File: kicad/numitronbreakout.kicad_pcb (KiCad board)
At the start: 2 copper layers, 25 parts, among them J1 Conn_01x06, U1 HV5812WG-G, U2 IV-12, U3 IV-12, U4 LM317_TO-220, U5 TPS61391RTER

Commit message: boost converter refactor
new design from web bench to reduce bom complexity & increase efficiency
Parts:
- removed Capd1: 470 pF, Capacitor_SMD:C_0402_1005Metric
- removed Cavcc1: 1.0 μF, Capacitor_SMD:C_0603_1608Metric
- removed Ccap1: 4.7 nF, Capacitor_SMD:C_0402_1005Metric
- removed Cin1: 1.0 μF, Capacitor_SMD:C_0402_1005Metric
- removed Cmon1, Cmon2: 10.0 pF, Capacitor_SMD:C_0201_0603Metric
- removed Cout1: 100 nF, Capacitor_SMD:C_0603_1608Metric
- removed D1: VF@Io = 1.0 V / VRRM = 100.0 V, Diode_SMD:D_SOD-123
- removed L1: 4.7 μH, Inductor_SMD:L_1008_2520Metric
- removed Ren1, Risshort1: 100 kΩ, Resistor_SMD:R_0402_1005Metric
- removed Rfbb1: 10 kΩ, Resistor_SMD:R_0402_1005Metric
- removed Rfbt1: 240 kΩ, Resistor_SMD:R_0603_1608Metric
- removed Rmon1, Rmon2: 3.01 kΩ, Resistor_SMD:R_0402_1005Metric
- removed Rvcc1: 10 Ω, Resistor_SMD:R_0402_1005Metric
- removed U5: TPS61391RTER, NewFootprints:RTE0016C
- added U7: LM2733XMF, Package_TO_SOT_SMD:SOT-23-5, F.Cu at (208.4, 71.5)
- moved U4 15.1 mm to (140.5, 63.4)
- moved R2 12.7 mm to (145.0, 70.0)
- moved R1 12.1 mm to (140.0, 70.0)
- moved J1 3.35 mm to (141.3, 53.0)
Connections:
- net V_in renamed V_out

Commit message: pcb layout
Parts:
- removed U7: LM2733XMF, Package_TO_SOT_SMD:SOT-23-5
- added Cf1: 100 pF, Capacitor_SMD:C_0805_2012Metric_Pad1.18x1.45mm_HandSolder, F.Cu at (200.0, 85.0)
- added Cin1: 2.2 μF, Capacitor_SMD:C_0603_1608Metric_Pad1.08x0.95mm_HandSolder, F.Cu at (210.0, 75.1)
- added Cout1: 4.7 μF, Capacitor_SMD:C_0805_2012Metric_Pad1.18x1.45mm_HandSolder, F.Cu at (200.0, 75.0)
- added D1: VF@Io = 550 mV, VRRM = 40 V, Diode_SMD:D_SOD-123F, F.Cu at (200.0, 70.0)
- added L1: 10 μH, NewFootprints:IND_TCK-146_TRP, F.Cu at (209.0, 70.0)
- added Rfbb1: 13.3 kΩ, Resistor_SMD:R_0402_1005Metric_Pad0.72x0.64mm_HandSolder, F.Cu at (205.0, 80.0)
- added Rfbt1: 316 kΩ, Resistor_SMD:R_0402_1005Metric_Pad0.72x0.64mm_HandSolder, F.Cu at (200.0, 80.0)
- added Rp1: 51.1 kΩ, Resistor_SMD:R_0402_1005Metric_Pad0.72x0.64mm_HandSolder, F.Cu at (209.9, 80.0)
- added U1: LM2733XMF, Package_TO_SOT_SMD:SOT-23-5, F.Cu at (205.1, 75.0)
- R1, R2: footprint Resistor_SMD:R_0402_1005Metric -> Resistor_SMD:R_0402_1005Metric_Pad0.72x0.64mm_HandSolder
- moved U4 19.8 mm to (165.0, 130.2)
- moved U5 19.8 mm to (135.0, 130.2)
- moved R1 17.6 mm to (157.6, 70.0)
- moved R2 17.5 mm to (162.5, 70.0)
- moved U2 17.0 mm to (157.5, 65.0)
- moved C1 16.9 mm to (135.0, 92.0)
- renumbered U4 to U2, U1 to U3, U2 to U4, U3 to U5
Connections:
- C1 pad 1: Boost Vin -> +30V
- C1 pad 2: V_out -> +30V
- J1 pad 7: Boost Vin -> +30V
- J1 pad 8: V_out -> +30V
- R2 pad 2: V_out -> +30V
- U2 pad 3: Boost Vin -> +30V
- U3 pad 1: Boost Vout -> +30V
- U3 pad 14: V_out -> +30V
- U3 pad 28: Boost Vin -> +30V
- U4 pad 3: V_out -> +30V
- U4 pad 4: Boost Vout -> +30V
- U5 pad 3: V_out -> +30V
- U5 pad 4: Boost Vout -> +30V
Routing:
- net Net-(U3-HVOUT1): track 0.00 -> 69.9 mm
- net Net-(U3-HVOUT17): track 0.00 -> 63.2 mm
- net Net-(U3-HVOUT2): track 0.00 -> 61.4 mm
- net Net-(U3-HVOUT16): track 0.00 -> 54.2 mm
- net Net-(U3-HVOUT3): track 0.00 -> 54.1 mm
- net Net-(U3-HVOUT4): track 0.00 -> 47.7 mm
- net Net-(U3-HVOUT15): track 0.00 -> 46.3 mm
- net Net-(U3-HVOUT5): track 0.00 -> 41.3 mm
- net Net-(U3-HVOUT14): track 0.00 -> 39.8 mm
- net Net-(U3-HVOUT6): track 0.00 -> 35.9 mm
- net Net-(U3-HVOUT13): track 0.00 -> 33.5 mm
- net Net-(U3-HVOUT11): track 0.00 -> 28.7 mm
- net Net-(U3-HVOUT12): track 0.00 -> 28.5 mm
- net Net-(U3-HVOUT7): track 0.00 -> 28.4 mm
- net Net-(U2-ADJ): track 0.00 -> 12.0 mm
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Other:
- copper layers 2 -> 4

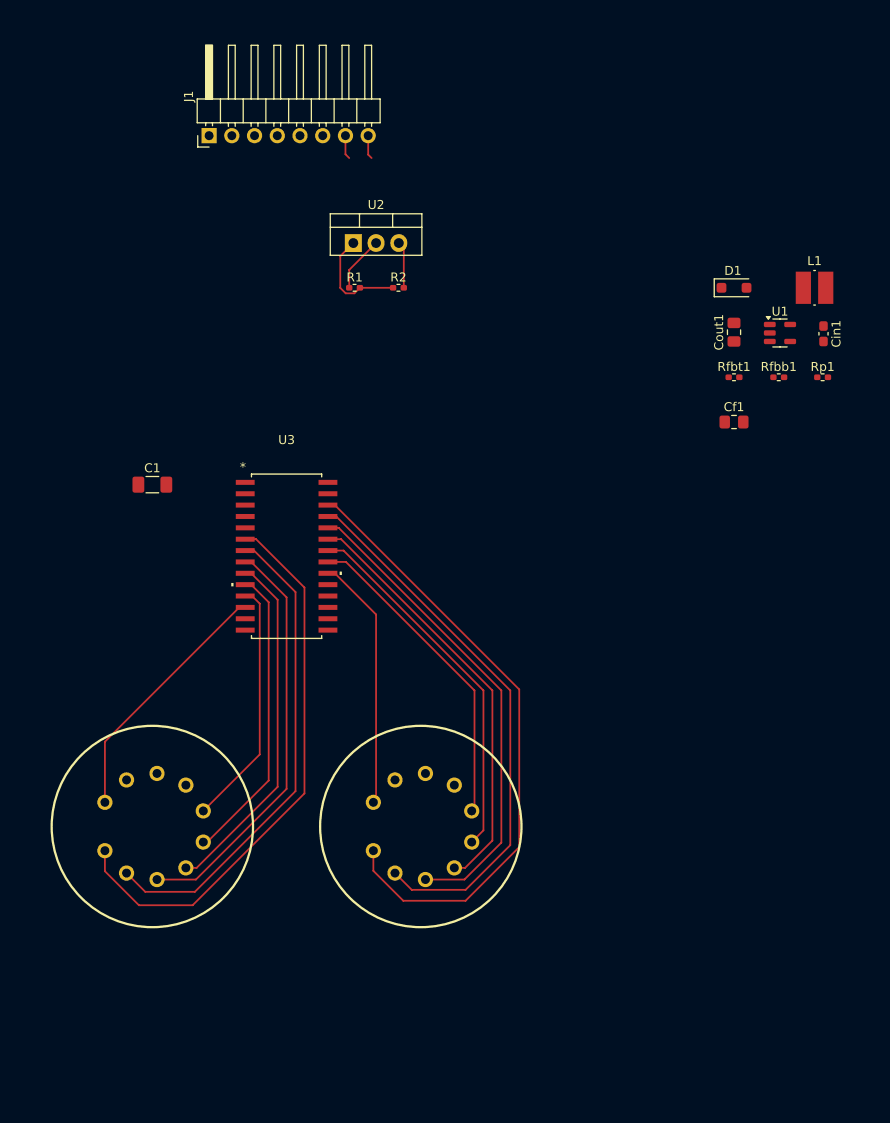
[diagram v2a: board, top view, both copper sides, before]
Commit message: finished wiring everything but 30v
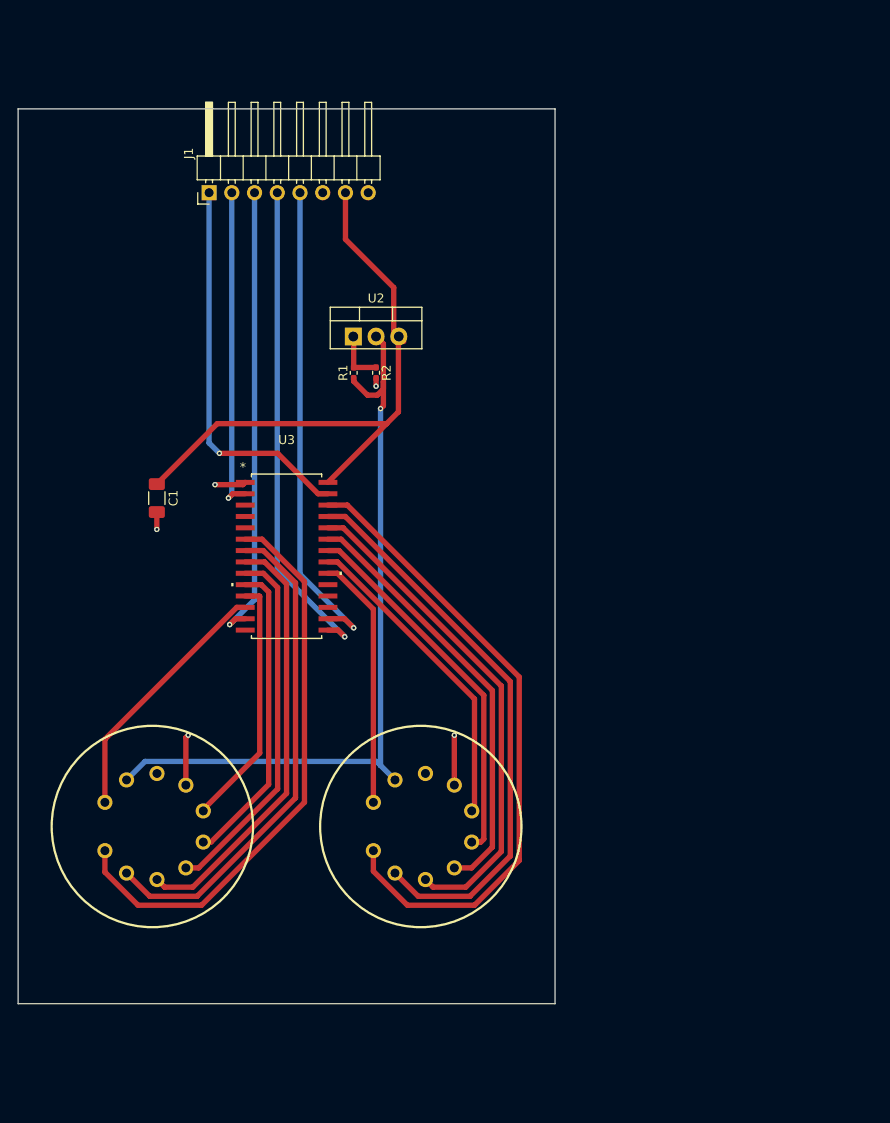
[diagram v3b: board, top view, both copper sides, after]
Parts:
- removed Cf1: 100 pF, Capacitor_SMD:C_0805_2012Metric_Pad1.18x1.45mm_HandSolder
- removed Cin1: 2.2 μF, Capacitor_SMD:C_0603_1608Metric_Pad1.08x0.95mm_HandSolder
- removed Cout1: 4.7 μF, Capacitor_SMD:C_0805_2012Metric_Pad1.18x1.45mm_HandSolder
- removed D1: VF@Io = 550 mV, VRRM = 40 V, Diode_SMD:D_SOD-123F
- removed L1: 10 μH, NewFootprints:IND_TCK-146_TRP
- removed Rfbb1: 13.3 kΩ, Resistor_SMD:R_0402_1005Metric_Pad0.72x0.64mm_HandSolder
- removed Rfbt1: 316 kΩ, Resistor_SMD:R_0402_1005Metric_Pad0.72x0.64mm_HandSolder
- removed Rp1: 51.1 kΩ, Resistor_SMD:R_0402_1005Metric_Pad0.72x0.64mm_HandSolder
- removed U1: LM2733XMF, Package_TO_SOT_SMD:SOT-23-5
- moved U2 10.4 mm to (157.5, 75.4)
- moved R2 9.82 mm to (160.0, 79.5), turned to -90 degrees
- moved R1 9.50 mm to (157.5, 79.5), turned to 90 degrees
- moved J1 6.38 mm to (141.3, 59.4)
- moved C1 1.58 mm to (135.5, 93.5), turned to -90 degrees
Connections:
- C1 pad 1: +30V -> +5V
- C1 pad 2: +30V -> GND
- J1 pad 7: +30V -> +5V
- J1 pad 8: +30V -> GND
- R2 pad 2: +30V -> GND
- U2 pad 3: +30V -> +5V
- U3 pad 14: +30V -> GND
- U3 pad 28: +30V -> +5V
- U4 pad 3: +30V -> GND
- U5 pad 3: +30V -> GND
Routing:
- net +1V5: track 6.24 -> 85.5 mm, vias 0 -> 1
- net +5V: track 0.00 -> 66.6 mm
- net +30V: track 10.6 -> 73.7 mm, vias 0 -> 3
- net CLOCK: track 0.00 -> 54.9 mm, vias 0 -> 1
- net STROBE: track 0.00 -> 54.4 mm, vias 0 -> 1
- net BLANKING: track 0.00 -> 51.4 mm, vias 0 -> 1
- net D_IN: track 0.00 -> 43.6 mm, vias 0 -> 1
- net D_OUT: track 0.00 -> 36.4 mm, vias 0 -> 1
- net Net-(U2-ADJ): track 12.0 -> 5.97 mm
- net GND: track 0.00 -> 2.84 mm, vias 0 -> 2
- net Net-(U3-HVOUT1): track 69.9 -> 72.1 mm
- net Net-(U3-HVOUT2): track 61.4 -> 63.3 mm
- net Net-(U3-HVOUT15): track 46.3 -> 48.2 mm
- net Net-(U3-HVOUT3): track 54.1 -> 55.7 mm
- net Net-(U3-HVOUT16): track 54.2 -> 55.7 mm
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- added copper zone on In1.Cu, net GND
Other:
- board outline added: 60 x 100 mm

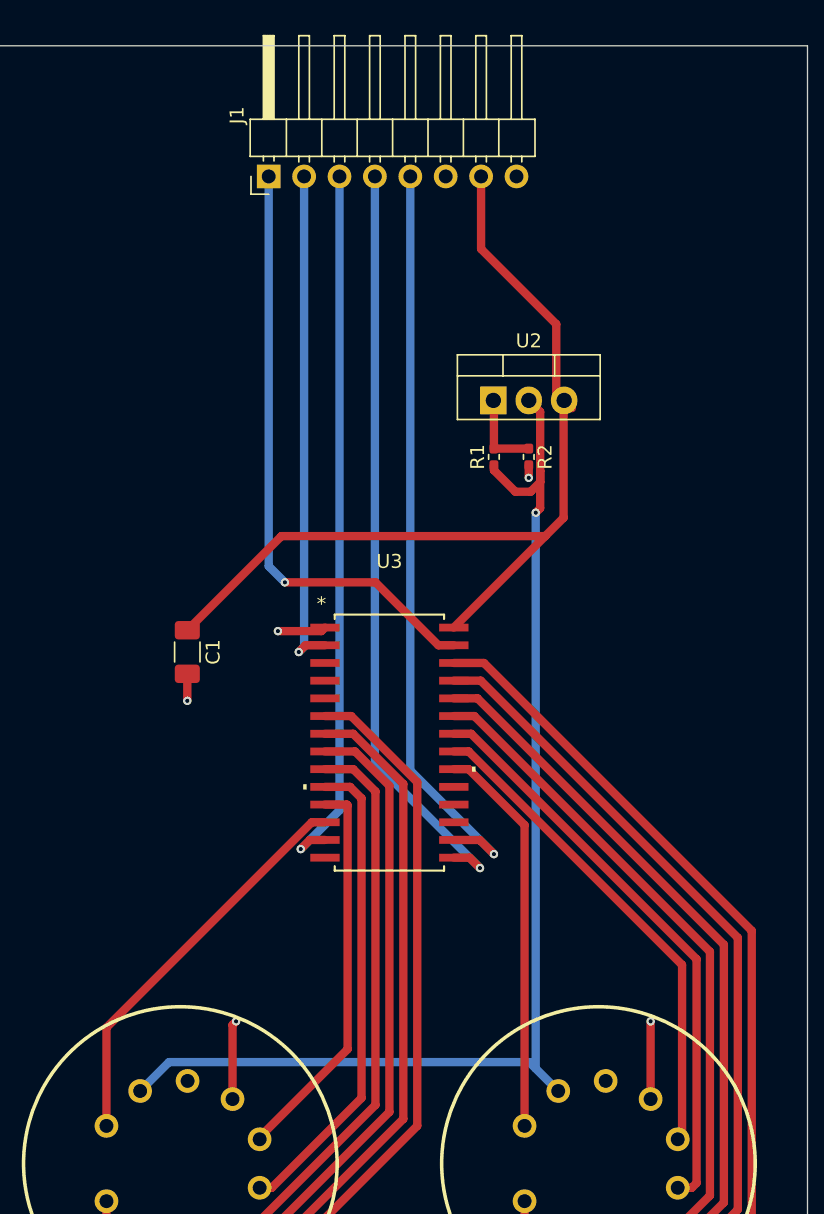
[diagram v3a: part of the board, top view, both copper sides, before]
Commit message: finally decided v boost solution, finished pathing pcb
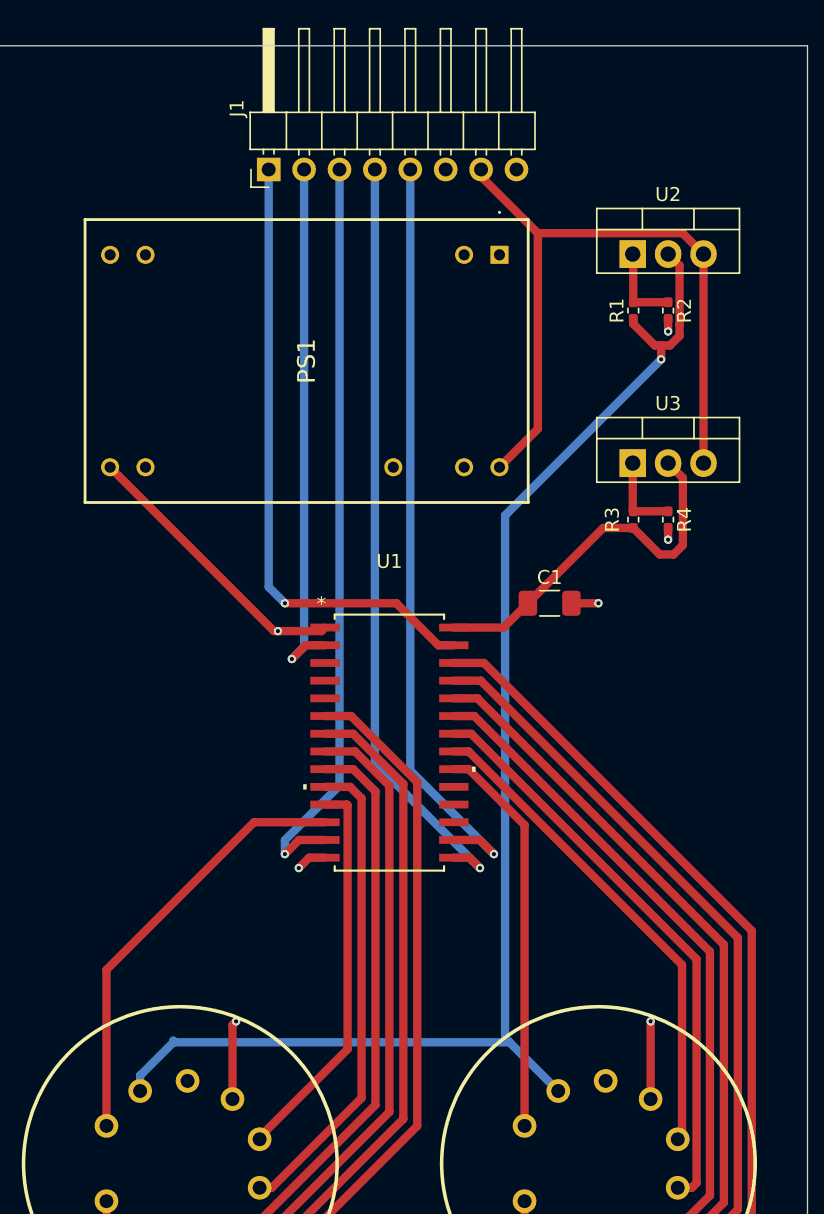
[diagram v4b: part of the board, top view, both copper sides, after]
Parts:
- added PS1: LDB-600L, NewFootprints:LDB600L, F.Cu at (157.9, 65.0)
- added R3: 330 Ω, Resistor_SMD:R_0402_1005Metric_Pad0.72x0.64mm_HandSolder, F.Cu at (167.5, 84.0)
- added R4: 1 kΩ, Resistor_SMD:R_0402_1005Metric_Pad0.72x0.64mm_HandSolder, F.Cu at (170.0, 84.0)
- added U3: LM317_TO-220, Package_TO_SOT_THT:TO-220-3_Vertical, F.Cu at (167.5, 79.9)
- R1: value 240 Ω -> 330 Ω
- R2: value 48 Ω -> 68 Ω
- moved C1 26.2 mm to (161.5, 90.0), turned to 0 degrees
- moved R1 14.5 mm to (167.5, 69.0)
- moved R2 14.5 mm to (170.0, 69.0)
- moved U2 14.5 mm to (167.5, 64.9)
- moved J1 0.50 mm to (141.3, 58.9)
- renumbered U3 to U1
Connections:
- J1 pad 7: +5V -> +12V
- U2 pad 3: +5V -> +12V
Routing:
- net +12V: track 0.00 -> 51.5 mm
- net +5V: track 66.6 -> 26.8 mm
- net +30V: track 73.7 -> 90.6 mm
- net +1V5: track 85.5 -> 99.3 mm
- net Net-(U3-ADJ): track 0.00 -> 5.97 mm
- net GND: track 2.84 -> 5.87 mm, vias 2 -> 4
- net Net-(U1-HVOUT11): track 28.8 -> 31.3 mm
- net BLANKING: track 51.4 -> 53.5 mm
- net D_OUT: track 36.4 -> 37.8 mm
- net D_IN: track 43.6 -> 44.5 mm

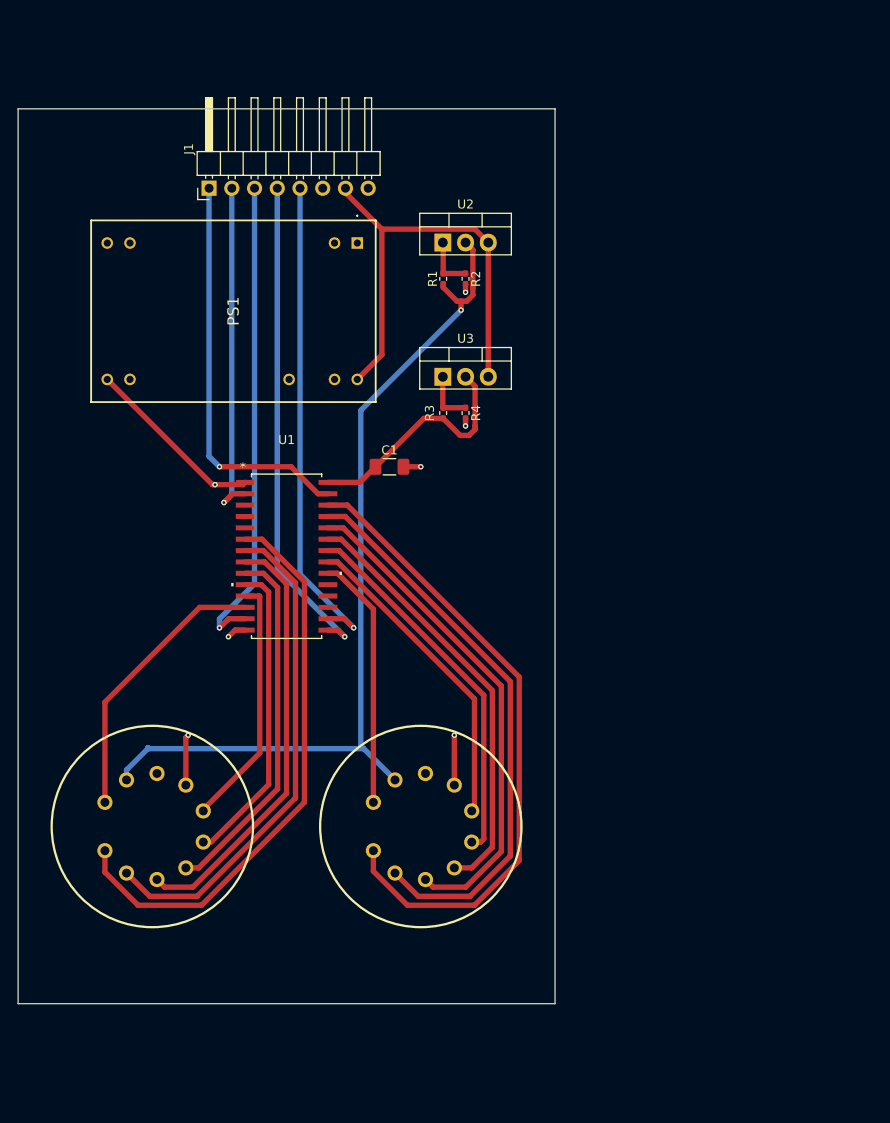
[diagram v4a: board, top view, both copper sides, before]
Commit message: increased resistor size, generated gerbers for fab
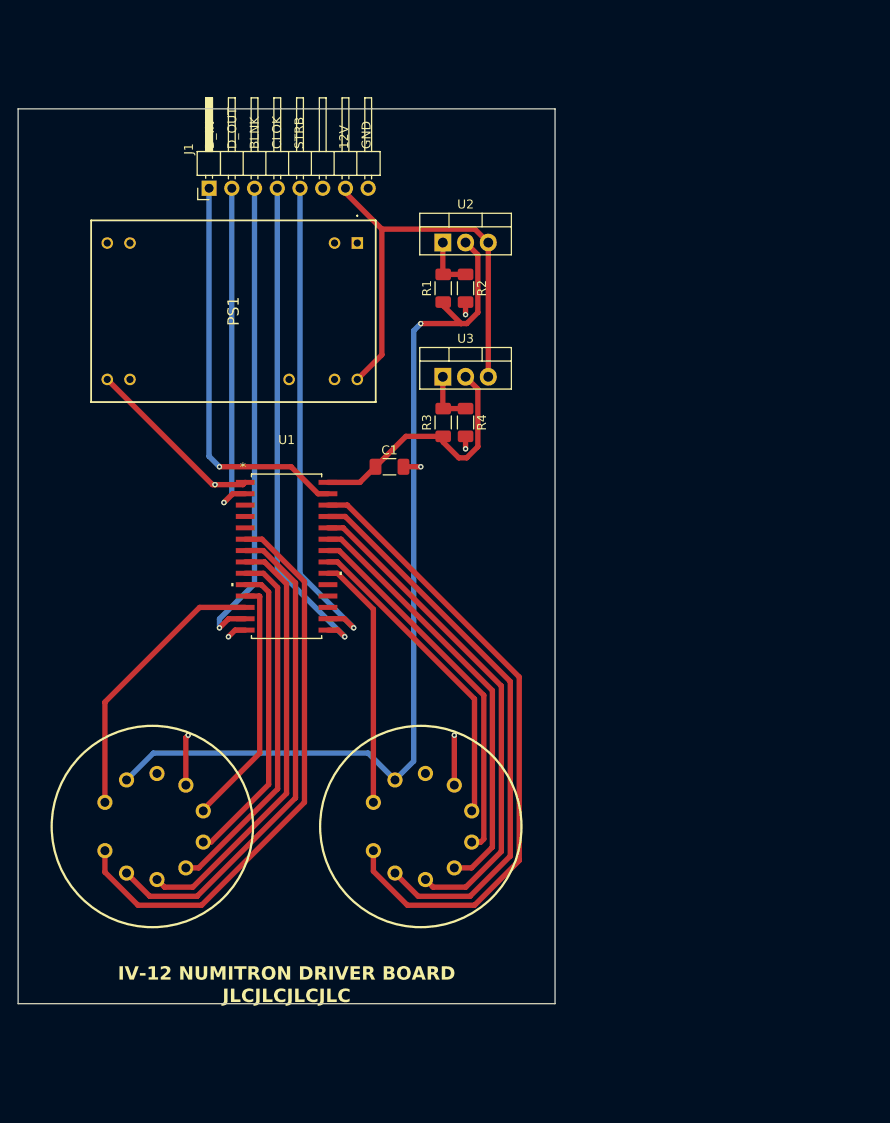
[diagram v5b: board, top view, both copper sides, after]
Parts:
- R1, R2, R3, R4: footprint Resistor_SMD:R_0402_1005Metric_Pad0.72x0.64mm_HandSolder -> Resistor_SMD:R_1206_3216Metric_Pad1.30x1.75mm_HandSolder
- moved R1 1.05 mm to (167.5, 70.0)
- moved R2 1.05 mm to (170.0, 70.0)
- moved R3 1.05 mm to (167.5, 85.0)
- moved R4 1.05 mm to (170.0, 85.0)
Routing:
- net +1V5: track 99.3 -> 103.2 mm
- net +5V: track 26.8 -> 29.2 mm
- net GND: track 5.87 -> 6.92 mm
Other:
- board text added: "12V"
- board text added: "BLNK"
- board text added: "CLOK"
- board text added: "D_IN"
- board text added: "D_OUT"
- board text added: "GND"
- board text added: "IV-12 NUMITRON DRIVER BOARD"
- board text added: "JLCJLCJLCJLC"
- board text added: "STRB"
